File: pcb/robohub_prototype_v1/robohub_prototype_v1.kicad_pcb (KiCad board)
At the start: 10 copper layers, 15 parts, among them J21 Barrel_Jack_Switch_Pin3Ring, J51 USB_A, J52 USB_A, U1 ATSAMA5D27C, U21 LM3880, U22 TPS564242DRL, U23 TPS564242DRL, U24 TPS564242DRL, U25 TPS564242DRL, U26 TPS564242DRL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

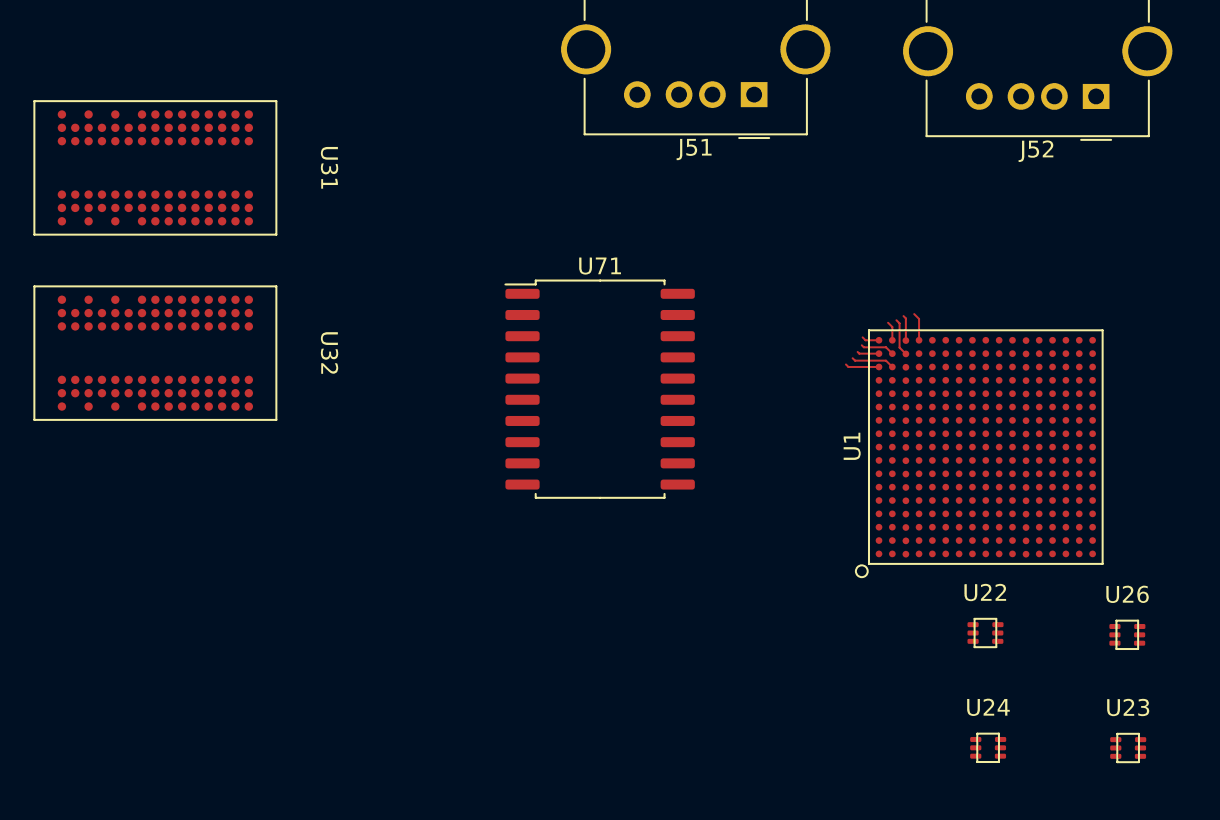
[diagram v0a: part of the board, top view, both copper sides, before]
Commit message: Update project to Kicad8. Update schematic, start fanning out BGA on PCB
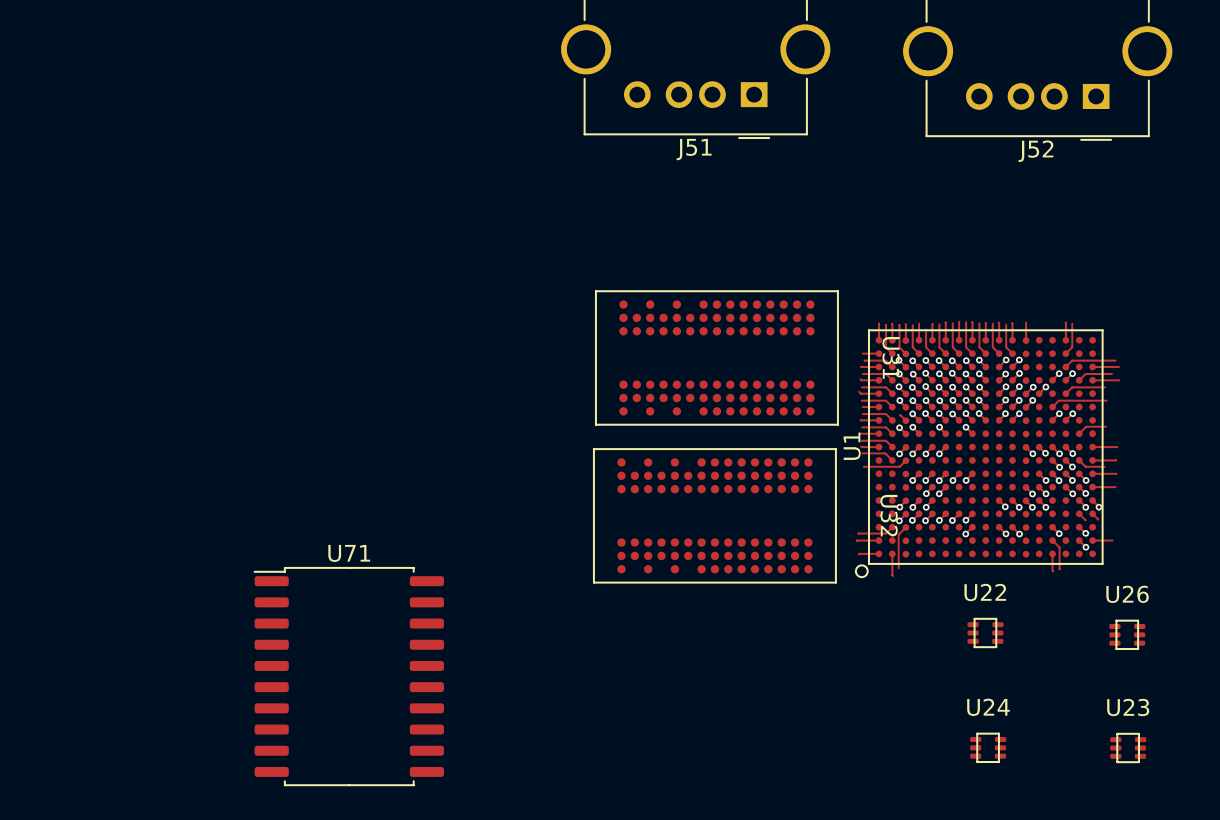
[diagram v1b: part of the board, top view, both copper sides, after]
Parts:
- moved U31 35.5 mm to (111.1, 88.9)
- moved U32 34.9 mm to (111.0, 98.3)
- moved U71 22.9 mm to (89.1, 108.0)
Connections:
- U1 pad N13: (no net) -> SD_VDD
- U1 pad P13: /MPU-SAMA5D27C_1/PC26_NC -> /MPU-SAMA5D27C_1/PA26_NC
- U1 pad R14: (no net) -> SD_VDD
- U1 pad R17: PA31 -> unconnected-(U1A-PA31-PadR17)
- U1 pad T15: /MPU-SAMA5D27C_1/PC24_NC -> /MPU-SAMA5D27C_1/PA24_NC
- U1 pad T16: /MPU-SAMA5D27C_1/PC27_NC -> /MPU-SAMA5D27C_1/PA27_NC
- U1 pad T17: PA29 -> unconnected-(U1A-PA29-PadT17)
- U1 pad U16: /MPU-SAMA5D27C_1/PC23_NC -> /MPU-SAMA5D27C_1/PA23_NC
- U1 pad U17: /MPU-SAMA5D27C_1/PC25_NC -> /MPU-SAMA5D27C_1/PA25_NC
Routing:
- net GND: track 0.00 -> 17.6 mm, vias 0 -> 28
- net SD_VDD: track 0.00 -> 5.37 mm, vias 0 -> 7
- net VCC_1_2: track 0.00 -> 4.87 mm, vias 0 -> 8
- net VCC_1_2_DDR: track 0.00 -> 4.16 mm, vias 0 -> 7
- net Net-(C328-Pad1): track 0.00 -> 3.90 mm
- net PA20_SD_DAT2: track 0.00 -> 3.39 mm
- net PA30_SD_DET_SW: track 0.00 -> 3.13 mm
- net /DDR2_3/DDR_DQM2: track 0.00 -> 2.66 mm
- net PB22_MDC: track 0.00 -> 2.63 mm
- net PA21_SD_DAT3: track 0.00 -> 2.50 mm
- net VCC_3_3_C: track 0.00 -> 2.43 mm, vias 0 -> 4
- net PB20_ETH_TX_D0: track 0.00 -> 2.19 mm
- net PA19_SD_DAT1: track 0.00 -> 2.10 mm
- net /DDR2_3/DDR_D0: track 0.00 -> 2.00 mm
- net /DDR2_3/DDR_D17: track 0.00 -> 1.98 mm
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
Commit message: Update paths to footprint libraries. Begin adding footprints for PDN resistors. Create master BOM
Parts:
- added R211: 36.5k, Resistor_SMD:R_0402_1005Metric, F.Cu at (114.0, 113.5)
- added R216: 36.5k, Resistor_SMD:R_0402_1005Metric, F.Cu at (114.0, 115.5)
- added R217: 10k, Resistor_SMD:R_0402_1005Metric, F.Cu at (114.0, 117.5)
- added R220: 36.5k, Resistor_SMD:R_0402_1005Metric, F.Cu at (114.0, 119.5)
- added R224: 36.5k, Resistor_SMD:R_0402_1005Metric, F.Cu at (114.0, 121.5)
- added R27: 36.5k, Resistor_SMD:R_0402_1005Metric, F.Cu at (114.0, 109.5)
- added R28: 135k, Resistor_SMD:R_0402_1005Metric, F.Cu at (114.0, 111.5)
- added U41: KSZ8081RNB, fryelabs:KSZ8081RNB, F.Cu at (184.4, 54.0)
- added U42: SI-60110-F, fryelabs:SI-60110-F, F.Cu at (172.2, 62.3)
- added U61: molex_5025700893, fryelabs:molex_5025700893, F.Cu at (170.8, 84.1)
- U1: footprint custom_footprint:SAMA5D27C-CNVAO -> fryelabs:ATSAMA5D27C
- U22, U23, U24, U25, U26, U27: footprint custom_footprint:TPS564247DRLR -> fryelabs:TPS564247DRLR
- U31, U32: footprint custom_footprint:W972GG6KB-25 -> fryelabs:W972GG6KB-25
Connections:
- net VDDBU renamed VCC_3_3_A

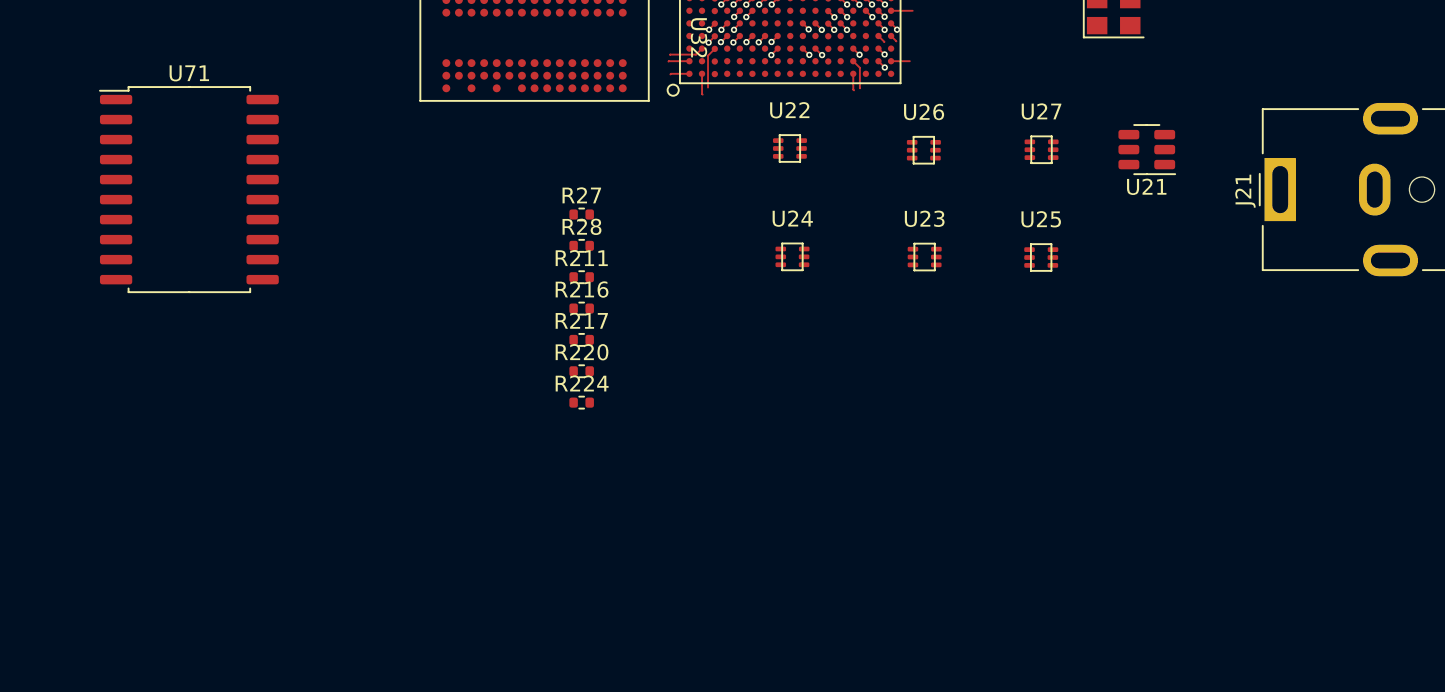
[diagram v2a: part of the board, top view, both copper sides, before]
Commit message: Begin PDN circuit design/BOM/layout
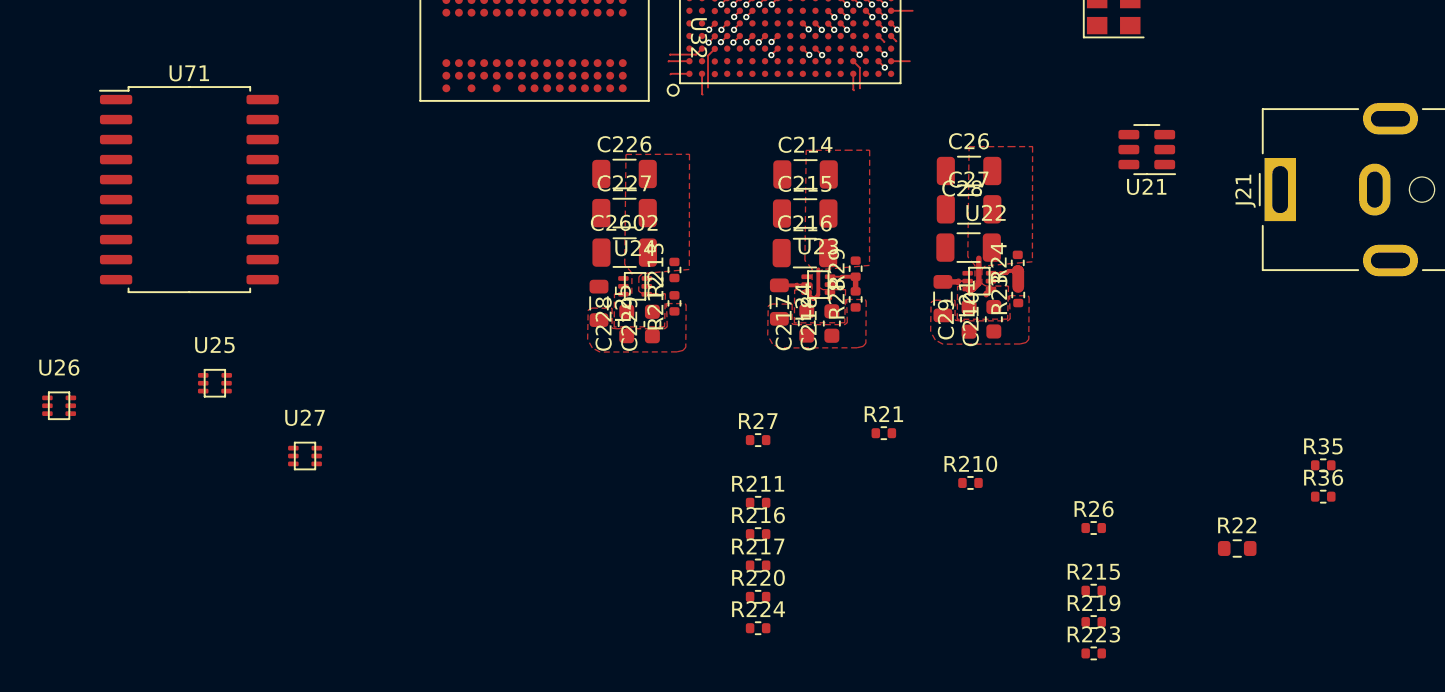
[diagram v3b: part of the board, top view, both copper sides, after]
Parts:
- added C210: 22u, Capacitor_SMD:C_0603_1608Metric, F.Cu at (140.2, 116.2)
- added C214: 10u, Capacitor_SMD:C_1206_3216Metric, F.Cu at (128.2, 107.0)
- added C215: 10u, Capacitor_SMD:C_1206_3216Metric, F.Cu at (128.2, 109.5)
- added C216: 0.1u, Capacitor_SMD:C_1206_3216Metric, F.Cu at (128.2, 112.0)
- added C217: 22u, Capacitor_SMD:C_0603_1608Metric, F.Cu at (128.3, 116.4)
- added C218: 22u, Capacitor_SMD:C_0603_1608Metric, F.Cu at (129.9, 116.5)
- added C226: 10u, Capacitor_SMD:C_1206_3216Metric, F.Cu at (116.7, 107.0)
- added C227: 10u, Capacitor_SMD:C_1206_3216Metric, F.Cu at (116.7, 109.4)
- added C228: 22u, Capacitor_SMD:C_0603_1608Metric, F.Cu at (116.8, 116.5)
- added C229: 22u, Capacitor_SMD:C_0603_1608Metric, F.Cu at (118.5, 116.5)
- added C26: 10u, Capacitor_SMD:C_1206_3216Metric, F.Cu at (138.6, 106.8)
- added C2602: 0.1u, Capacitor_SMD:C_1206_3216Metric, F.Cu at (116.7, 112.0)
- added C27: 10u, Capacitor_SMD:C_1206_3216Metric, F.Cu at (138.6, 109.2)
- added C28: 0.1u, Capacitor_SMD:C_1206_3216Metric, F.Cu at (138.6, 111.6)
- added C29: 22u, Capacitor_SMD:C_0603_1608Metric, F.Cu at (138.6, 116.2)
- added L21: 0.82u, Inductor_SMD:L_0805_2012Metric, F.Cu at (136.9, 114.9)
- added L24: 0.82u, Inductor_SMD:L_0805_2012Metric, F.Cu at (126.5, 115.1)
- added L25: 0.82u, Inductor_SMD:L_0805_2012Metric, F.Cu at (115.1, 115.2)
- added R21: 100k, Resistor_SMD:R_0402_1005Metric, F.Cu at (133.2, 123.4)
- added R210: 100k, Resistor_SMD:R_0402_1005Metric, F.Cu at (138.7, 126.6)
- added R212: 100k, Resistor_SMD:R_0402_1005Metric, F.Cu at (119.9, 115.2)
- added R213: 22.1k, Resistor_SMD:R_0402_1005Metric, F.Cu at (119.9, 113.0)
- added R215: 100k, Resistor_SMD:R_0402_1005Metric, F.Cu at (146.5, 133.4)
- added R219: 100k, Resistor_SMD:R_0402_1005Metric, F.Cu at (146.5, 135.4)
- added R22: 36.5k, Resistor_SMD:R_0603_1608Metric, F.Cu at (155.6, 130.7)
- added R223: 100k, Resistor_SMD:R_0402_1005Metric, F.Cu at (146.5, 137.4)
- added R23: 100k, Resistor_SMD:R_0402_1005Metric, F.Cu at (141.7, 114.6)
- added R24: 22.1k, Resistor_SMD:R_0402_1005Metric, F.Cu at (141.7, 112.6)
- added R26: 100k, Resistor_SMD:R_0402_1005Metric, F.Cu at (146.5, 129.4)
- added R29: 22.1k, Resistor_SMD:R_0402_1005Metric, F.Cu at (131.4, 113.0)
- added R35: 100k, Resistor_SMD:R_0402_1005Metric, F.Cu at (161.1, 125.5)
- added R36: 100k, Resistor_SMD:R_0402_1005Metric, F.Cu at (161.1, 127.4)
- R28: value 135k -> 100k
- U1: footprint fryelabs:ATSAMA5D27C -> fryelabs_kicad_footprint_lib:ATSAMA5D27C
- U22, U23, U24, U25, U26, U27: footprint fryelabs:TPS564247DRLR -> fryelabs_kicad_footprint_lib:TPS564247DRLR
- U31, U32: footprint fryelabs:W972GG6KB-25 -> fryelabs_kicad_footprint_lib:W972GG6KB-25
- U41: footprint fryelabs:KSZ8081RNB -> fryelabs_kicad_footprint_lib:KSZ8081RNB
- U42: footprint fryelabs:SI-60110-F -> fryelabs_kicad_footprint_lib:SI-60110-F
- U61: footprint fryelabs:molex_5025700893 -> fryelabs_kicad_footprint_lib:molex_5025700893
- moved U26 57.2 mm to (80.8, 121.7)
- moved U25 53.1 mm to (90.7, 120.2)
- moved U27 50.6 mm to (96.4, 124.9)
- moved R217 18.2 mm to (125.2, 131.8)
- moved R220 18.2 mm to (125.2, 133.8)
- moved R211 18.2 mm to (125.2, 127.8)
- moved R216 18.2 mm to (125.2, 129.8)
- moved R224 18.2 mm to (125.2, 135.8)
- moved R27 18.2 mm to (125.2, 123.8)
- moved R28 17.7 mm to (131.4, 114.9), turned to 90 degrees
- moved U22 14.7 mm to (139.2, 113.8)
- moved U24 10.2 mm to (117.4, 114.1)
- moved U23 6.97 mm to (129.0, 114.0)
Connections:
- net Net-(D22-K) renamed /Power Managment_2/VCC_3_3B_EN
- net Net-(D23-K) renamed /Power Managment_2/VCC_3_3C_EN
- net Net-(U23-FB) renamed /Power Managment_2/VCC_3_3_B_FB
- net VCC_3_3_A renamed VDDBU
- U22 pad 2: Net-(U22-SW) -> /Power Managment_2/VCC_3_3_A_SW
- U22 pad 5: Net-(D21-K) -> /Power Managment_2/VCC_3A_EN
- U22 pad 6: Net-(U22-FB) -> /Power Managment_2/VCC_3_3_A_FB
- U23 pad 2: Net-(U23-SW) -> /Power Managment_2/VCC_3_3_B_SW
- U24 pad 2: Net-(U24-SW) -> /Power Managment_2/VCC_3_3_C_SW
- U24 pad 6: Net-(U24-FB) -> /Power Managment_2/VCC_3_3_C_FB
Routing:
- net GND: track 17.6 -> 24.0 mm
- net /Power Managment_2/VCC_3_3_A_FB: track 0.00 -> 2.78 mm
- net /Power Managment_2/VCC_3_3_B_FB: track 0.00 -> 2.55 mm
- net /Power Managment_2/VCC_3_3_B_SW: track 0.00 -> 1.75 mm
- net /Power Managment_2/VCC_3_3_A_SW: track 0.00 -> 1.59 mm
- added copper zone on F.Cu, net (none)
- added copper zone on F.Cu, net GND
- added copper zone on F.Cu, net VDDBU
